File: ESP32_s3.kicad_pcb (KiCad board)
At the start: 2 copper layers, 72 parts, among them J11 backup, J13 Jetson Power Supply, J13 jetsonnano, J14 TXRX, J15 TXRX2, J3 Conn_01x02, J4 Servo motor, J5 PJ-040DH, J7 Conn_01x02, J8 Conn_01x02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

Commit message: update traces
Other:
- board outline added: 100 x 75 mm
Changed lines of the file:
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@@
 	)
 	(setup
+		(stackup
+			(layer "F.SilkS"
+				(type "Top Silk Screen")
+			)
+			(layer "F.Paste"
+				(type "Top Solder Paste")
+			)
+			(layer "F.Mask"
+				(type "Top Solder Mask")
+				(thickness 0.01)
+			)
+			(layer "F.Cu"
+				(type "copper")
+				(thickness 0.035)
+			)
+			(layer "dielectric 1"
+				(type "core")
+				(thickness 1.51)
+				(material "FR4")
+				(epsilon_r 4.5)
+				(loss_tangent 0.02)
+			)
+			(layer "B.Cu"
+				(type "copper")
+				(thickness 0.035)
+			)
+			(layer "B.Mask"
+				(type "Bottom Solder Mask")
+				(thickness 0.01)
+			)
+			(layer "B.Paste"
+				(type "Bottom Solder Paste")
+			)
+			(layer "B.SilkS"
+				(type "Bottom Silk Screen")
+			)
+			(copper_finish "None")
+			(dielectric_constraints no)
+		)
 		(pad_to_mask_clearance 0)
 		(allow_soldermask_bridges_in_footprints no)
@@
 		(descr "<B>WR-PHD </B><BR> 2.54mm Pin Header, 3 Pin")
 		(property "Reference" "J13"
-			(at -6.6096 -0.6625 0)
+			(at -5.31 0.02 0)
 			(layer "F.SilkS")
 			(effects
@@
 		(descr "<B>WR-PHD </B><BR> 2.54mm Pin Header, 3 Pin")
 		(property "Reference" "J4"
-			(at -6.6096 -0.6625 0)
+			(at -5.02 -0.48 0)
 			(layer "F.SilkS")
 			(effects
@@
 	)
 	(gr_rect
-		(start 105.46 55)
-		(end 205.46 130)
+		(start 105 55)
+		(end 205 130)
 		(stroke
-			(width 0.2)
+			(width 0.05)
 			(type default)
 		)
 		(fill none)
-		(layer "F.Cu")
-		(net 16)
+		(layer "Edge.Cuts")
 	)
 	(segment
@@
 		(start 112.34 116.615)
 		(end 112.34 115.447)
-		(width 0.2)
+		(width 0.254)
 		(layer "F.Cu")
 		(net 1)
@@
 		(start 112.34 118.115)
 		(end 112.34 116.615)
-		(width 0.2)
+		(width 0.254)
 		(layer "F.Cu")
 		(net 1)
@@
 		(start 112.34 116.615)
 		(end 110.84 115.115)
-		(width 0.2)
+		(width 0.381)
 		(layer "F.Cu")
 		(net 1)
@@
 		(start 130.46 70.375)
 		(end 123.8325 70.375)
-		(width 0.2)
+		(width 0.254)
 		(layer "F.Cu")
 		(net 2)
@@
 		(start 123.8325 70.375)
 		(end 119.9575 66.5)
-		(width 0.2)
+		(width 0.254)
 		(layer "F.Cu")
 		(net 2)
@@
 		(start 124.36 64.5)
 		(end 119.9575 64.5)
-		(width 0.2)
+		(width 0.254)
 		(layer "F.Cu")
 		(net 19)
@@
 		(start 130.46 66)
 		(end 130.46 68.5)
-		(width 0.2)
+		(width 0.254)
 		(layer "F.Cu")
 		(net 35)
@@
 		(start 126.96 64)
 		(end 126.46 64.5)
-		(width 0.2)
+		(width 0.381)
 		(layer "F.Cu")
 		(net 71)
@@
 		(start 130.46 64)
 		(end 130.46 58.5)
-		(width 0.2)
+		(width 0.381)
 		(layer "F.Cu")
 		(net 71)
@@
 		(start 130.46 64)
 		(end 126.96 64)
-		(width 0.2)
+		(width 0.381)
 		(layer "F.Cu")
 		(net 71)
@@
 		(start 130.46 58.5)
 		(end 133 58.5)
-		(width 0.2)
+		(width 0.381)
 		(layer "B.Cu")
 		(net 71)

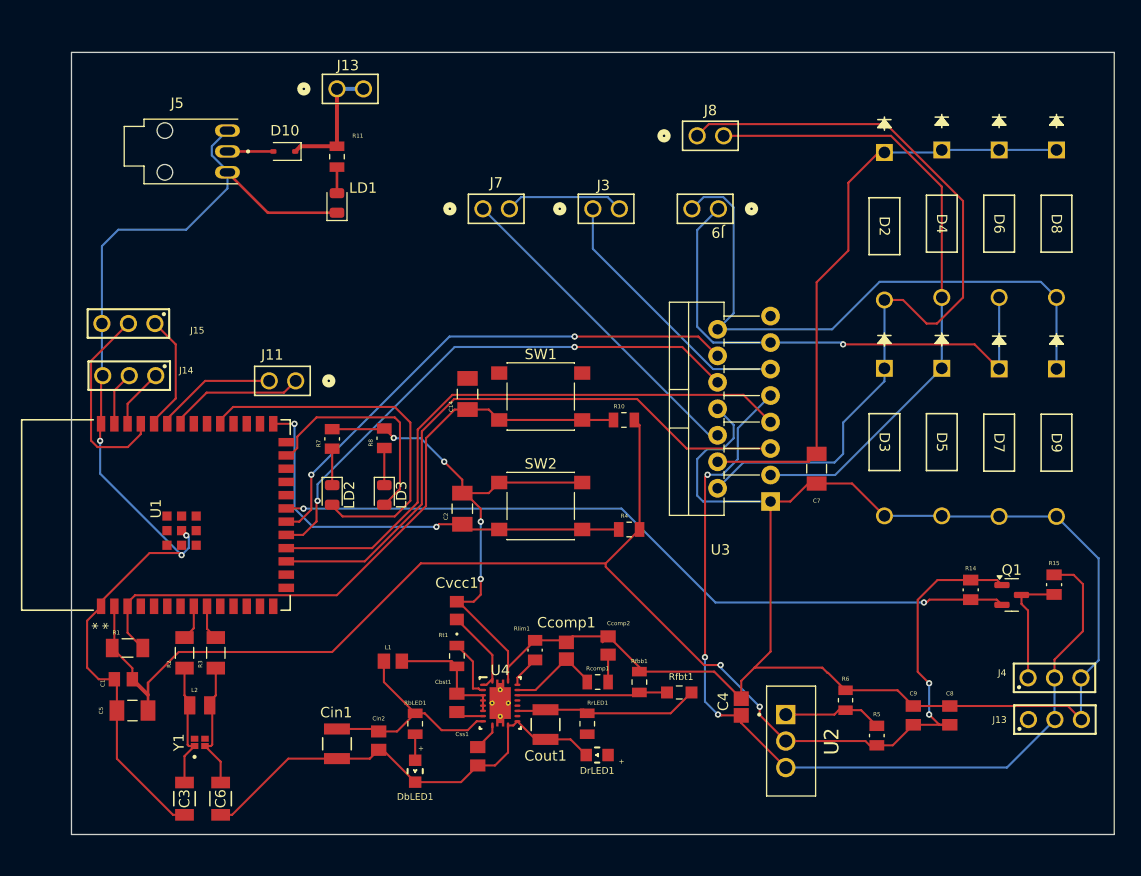
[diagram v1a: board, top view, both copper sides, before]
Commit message: update drill holes and name
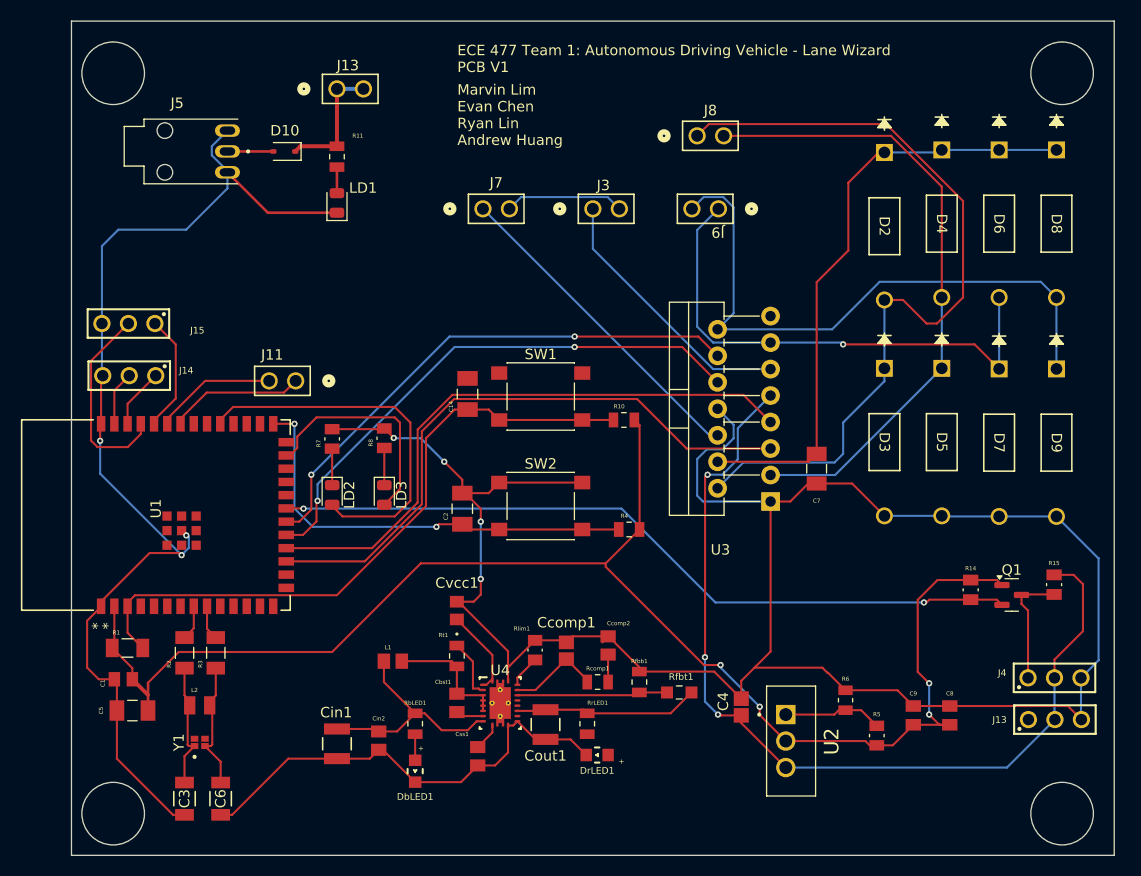
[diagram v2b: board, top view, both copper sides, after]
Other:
- board size 100 x 75 mm -> 100 x 80 mm
- board text added: "ECE 477 Team 1: Autonomous Driving Vehicle - Lane Wizard PCB V1"
- board text added: "Marvin Lim Evan Chen Ryan Lin Andrew Huang"
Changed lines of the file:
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@@
 		)
 	)
-	(gr_rect
-		(start 105 55)
-		(end 205 130)
+	(gr_circle
+		(center 109 128)
+		(end 112 128)
 		(stroke
 			(width 0.05)
@@
 		(layer "Edge.Cuts")
 	)
+	(gr_circle
+		(center 200 128)
+		(end 203 128)
+		(stroke
+			(width 0.05)
+			(type default)
+		)
+		(fill none)
+		(layer "Edge.Cuts")
+	)
+	(gr_circle
+		(center 200 57)
+		(end 203 57)
+		(stroke
+			(width 0.05)
+			(type default)
+		)
+		(fill none)
+		(layer "Edge.Cuts")
+	)
+	(gr_rect
+		(start 105 52)
+		(end 205 132)
+		(stroke
+			(width 0.05)
+			(type default)
+		)
+		(fill none)
+		(layer "Edge.Cuts")
+	)
+	(gr_circle
+		(center 109 57)
+		(end 112 57)
+		(stroke
+			(width 0.05)
+			(type default)
+		)
+		(fill none)
+		(layer "Edge.Cuts")
+	)
+	(gr_text "ECE 477 Team 1: Autonomous Driving Vehicle - Lane Wizard\nPCB V1\n"
+		(at 142 57 0)
+		(layer "F.SilkS")
+		(effects
+			(font
+				(size 1 1)
+				(thickness 0.1)
+			)
+			(justify left bottom)
+		)
+	)
+	(gr_text "Marvin Lim\nEvan Chen\nRyan Lin\nAndrew Huang"
+		(at 142 64 0)
+		(layer "F.SilkS")
+		(effects
+			(font
+				(size 1 1)
+				(thickness 0.1)
+			)
+			(justify left bottom)
+		)
+	)
 	(segment

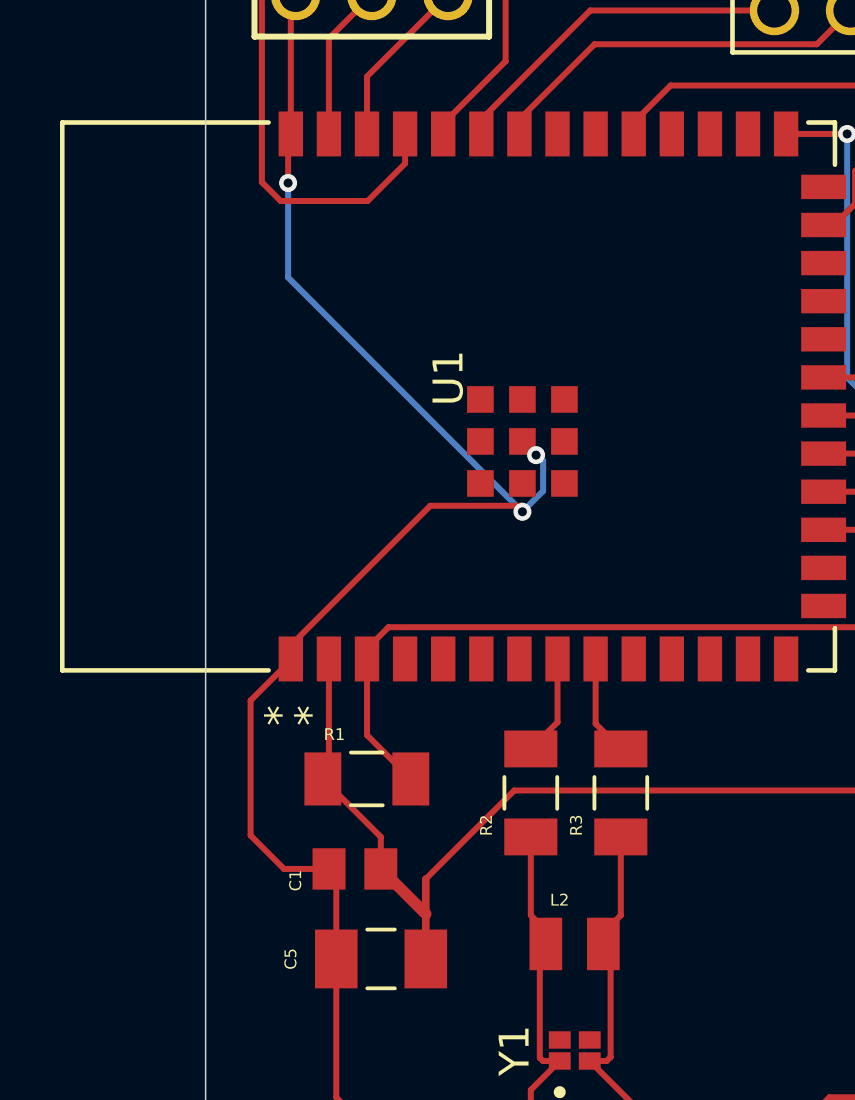
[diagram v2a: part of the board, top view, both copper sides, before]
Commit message: fix acute angles
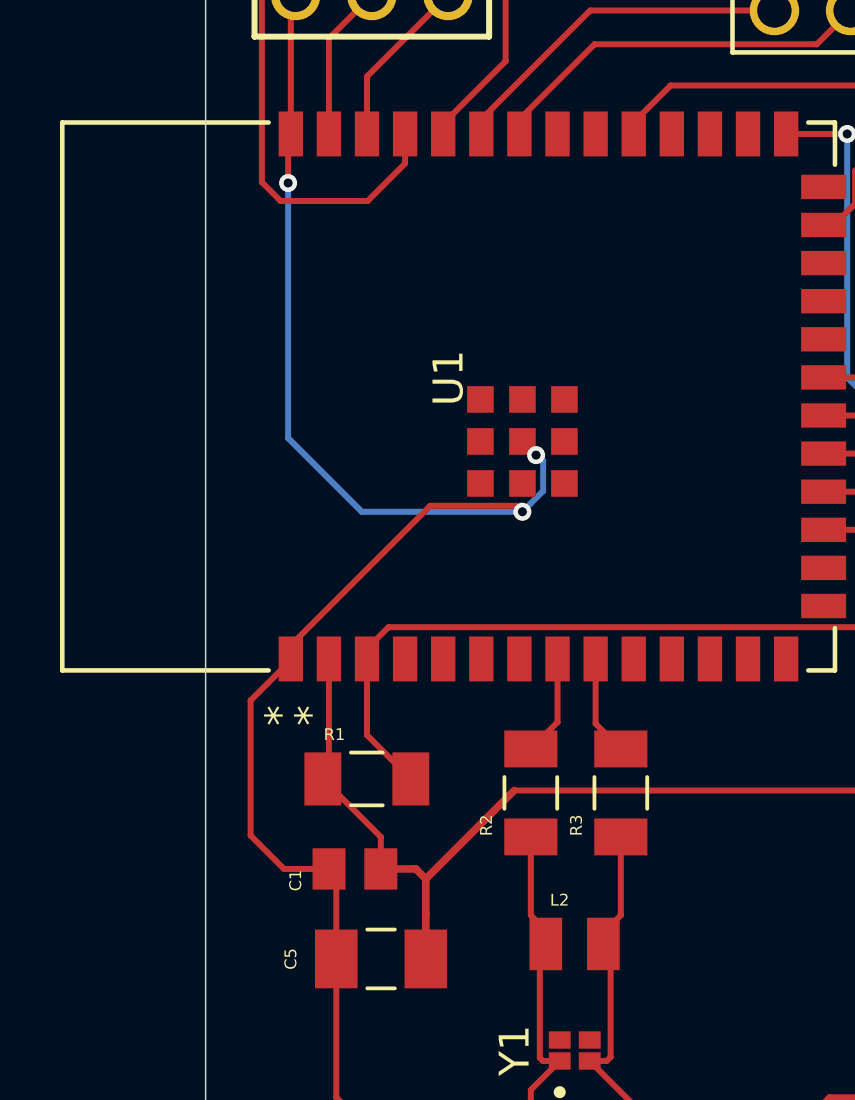
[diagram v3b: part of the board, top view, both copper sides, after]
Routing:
- net GND: track 351.1 -> 354.2 mm
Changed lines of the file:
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@@
+		)
+	)
+	(gr_text_box "Boost Voltage Regulator"
+		(start 141.5 126)
+		(end 162.5 129)
+		(layer "F.SilkS")
+		(effects
+			(font
+				(size 1 1)
+				(thickness 0.1)
+			)
+			(justify left top)
+		)
+		(border yes)
+		(stroke
+			(width 0.1)
+			(type solid)
+		)
+	)
+	(gr_text_box "micro"
+		(start 122.25 79)
+		(end 127.75 82)
+		(layer "F.SilkS")
+		(effects
+			(font
+				(size 1 1)
+				(thickness 0.1)
+			)
+			(justify left top)
+		)
+		(border yes)
+		(stroke
+			(width 0.1)
+			(type solid)
+		)
+	)
+	(gr_text_box "Logic Level Shifter"
+		(start 181 101)
+		(end 198 104)
+		(layer "F.SilkS")
+		(effects
+			(font
+				(size 1 1)
+				(thickness 0.1)
+			)
+			(justify left top)
+		)
+		(border yes)
+		(stroke
+			(width 0.1)
+			(type solid)
+		)
+	)
+	(gr_text_box "Switch"
+		(start 145 79)
+		(end 151 82)
+		(layer "F.SilkS")
+		(effects
+			(font
+				(size 1 1)
+				(thickness 0.1)
+			)
+			(justify left top)
+		)
+		(border yes)
+		(stroke
+			(width 0.1)
+			(type solid)
+		)
+	)
+	(gr_text_box "Power Supply"
+		(start 114.5 55)
+		(end 126.5 58)
+		(layer "F.SilkS")
+		(effects
+			(font
+				(size 1 1)
+				(thickness 0.1)
+			)
+			(justify left top)
+		)
+		(border yes)
+		(stroke
+			(width 0.1)
+			(type solid)
+		)
+	)
+	(gr_text_box "H-Bridge"
+		(start 164.5 74)
+		(end 173.5 77)
+		(layer "F.SilkS")
+		(effects
+			(font
+				(size 1 1)
+				(thickness 0.1)
+			)
+			(justify left top)
+		)
+		(border yes)
+		(stroke
+			(width 0.1)
+			(type solid)
+		)
+	)
+	(gr_text_box "Low Dropout"
+		(start 178 126)
+		(end 189 129)
+		(layer "F.SilkS")
+		(effects
+			(font
+				(size 1 1)
+				(thickness 0.1)
+			)
+			(justify left top)
+		)
+		(border yes)
+		(stroke
+			(width 0.1)
+			(type solid)
 		)
 	)
@@
 		(end 109.11 108.115)
 		(width 0.2)
+		(layer "F.Cu")
+		(net 1)
+	)
+	(segment
+		(start 112.008 115.115)
+		(end 112.34 115.447)
+		(width 0.254)
 		(layer "F.Cu")
 		(net 1)
@@
 		(start 112.34 115.447)
 		(end 115.287 112.5)
-		(width 0.2)
+		(width 0.254)
 		(layer "F.Cu")
 		(net 1)
@@
 		(end 181.55 121.45)
 		(width 0.2)
+		(layer "F.Cu")
+		(net 1)
+	)
+	(segment
+		(start 110.84 115.115)
+		(end 112.008 115.115)
+		(width 0.254)
 		(layer "F.Cu")
 		(net 1)
@@
 		(end 194.23 106.08)
 		(width 0.2)
-		(layer "F.Cu")
-		(net 1)
-	)
-	(segment
-		(start 112.34 116.615)
-		(end 110.84 115.115)
-		(width 0.381)
 		(layer "F.Cu")
 		(net 1)
@@
 	)
 	(segment
+		(start 107.75 100.75)
+		(end 110.209502 103.209502)
+		(width 0.2)
+		(layer "B.Cu")
+		(net 2)
+	)
+	(segment
 		(start 118.4575 64)
 		(end 119.9575 62.5)
@@
 	)
 	(segment
-		(start 115.56 103.209502)
-		(end 107.75 95.399502)
-		(width 0.2)
-		(layer "B.Cu")
-		(net 2)
-	)
-	(segment
 		(start 140.75 94.25)
 		(end 138.5 92)
@@
 	)
 	(segment
+		(start 110.209502 103.209502)
+		(end 115.56 103.209502)
+		(width 0.2)
+		(layer "B.Cu")
+		(net 2)
+	)
+	(segment
 		(start 138.5 92)
 		(end 135.927493 92)
@@
 	)
 	(segment
-		(start 107.75 95.399502)
-		(end 107.75 92.25)
-		(width 0.2)
-		(layer "B.Cu")
-		(net 2)
-	)
-	(segment
 		(start 109.5 72)
 		(end 116 72)
 		(width 0.2)
 		(layer "B.Cu")
+		(net 2)
+	)
+	(segment
+		(start 107.75 92.25)
+		(end 107.75 100.75)
+		(width 0.2)
+		(layer "B.Cu")

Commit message: update traces
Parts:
- moved RrLED1 3.54 mm to (158.0, 119.2)
- moved DrLED1 2.60 mm to (154.2, 120.0), turned to 90 degrees
- moved RbLED1 1.62 mm to (138.0, 121.0)
- moved DbLED1 1.52 mm to (138.0, 125.5)
- moved R6 1.38 mm to (179.2, 118.5)
- moved Cbst1 0.50 mm to (142.0, 116.9)
- moved C3 0.34 mm to (115.5, 126.5)
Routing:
- net Net-(DrLED1-A): track 0.00 -> 4.27 mm
- net GND: track 354.2 -> 357.8 mm
- net Vin: track 22.1 -> 21.5 mm
- net +3.3V: track 140.9 -> 141.4 mm
- added copper zone on F.Cu, net +3.3V
- added copper zone on F.Cu, net +5V
- added copper zone on F.Cu, net GND
- added copper zone on F.Cu, net Vin
- added copper zone on F.Cu, net Vout

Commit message: add pig
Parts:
- moved LD1 7.22 mm to (123.2, 69.0)
- moved R11 7.22 mm to (123.2, 64.6)
- moved D10 7.22 mm to (118.2, 64.1)
- moved J13 6.77 mm to (130.0, 65.2)
- moved J5 6.48 mm to (113.5, 64.0)
- moved J8 6.39 mm to (171.2, 64.5)
- moved C6 0.30 mm to (119.0, 126.5)
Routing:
- net GND: track 357.8 -> 351.4 mm
- net Net-(D4-A): track 61.0 -> 55.4 mm
- net Net-(D2-A): track 77.6 -> 72.1 mm
- net 5V: track 12.2 -> 14.2 mm
- net Net-(D10-A): track 4.40 -> 3.68 mm
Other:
- outline, holes or cut-outs redrawn

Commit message: fix error
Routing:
- net GND: track 351.4 -> 381.4 mm, vias 7 -> 11
- net Vout: track 17.6 -> 18.6 mm

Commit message: update schematic and PCB
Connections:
- C7 pad 1: +12V -> Vout
- D2 pad 1: +12V -> Vout
- D4 pad 1: +12V -> Vout
- D6 pad 1: +12V -> Vout
- D8 pad 1: +12V -> Vout
- U3 pad 4: +12V -> Vout
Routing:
- net Vout: track 18.6 -> 100.8 mm, vias 0 -> 2
- net +12V: track 58.3 -> 0.00 mm

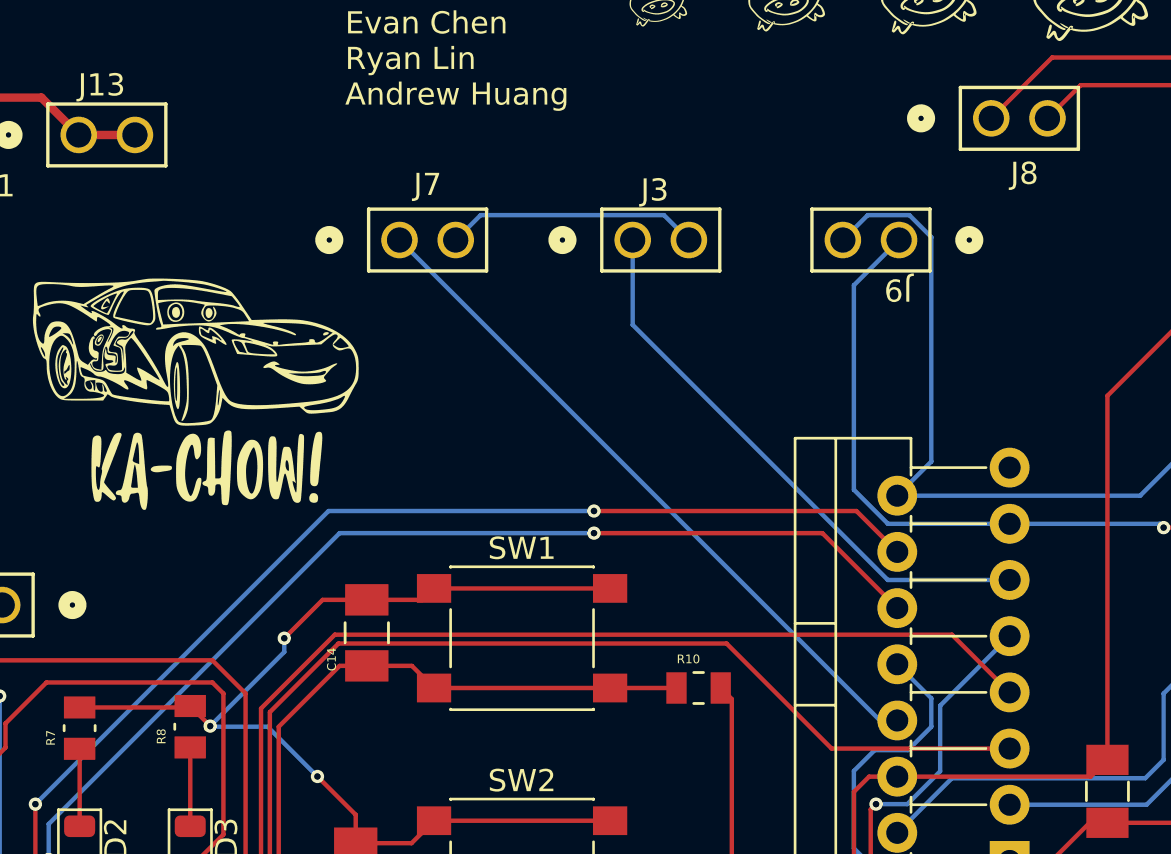
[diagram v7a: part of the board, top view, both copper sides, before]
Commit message: update labels and traces
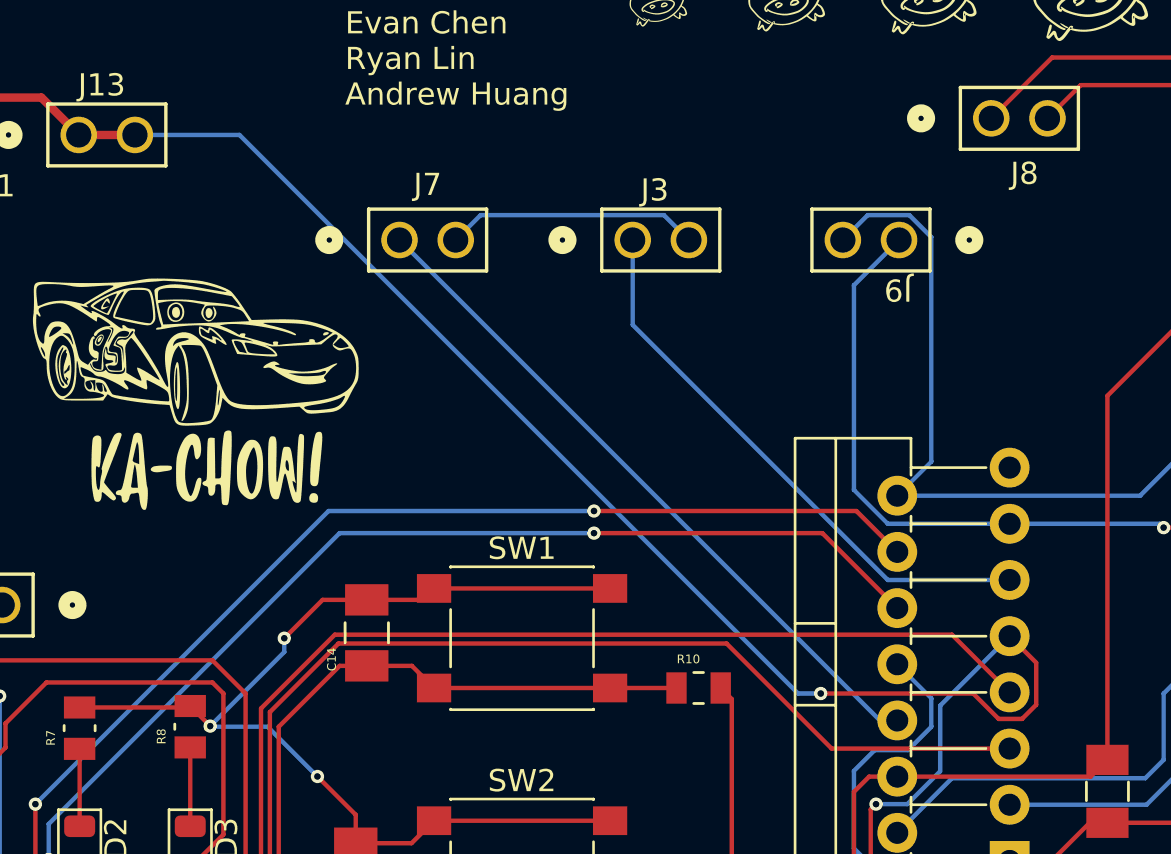
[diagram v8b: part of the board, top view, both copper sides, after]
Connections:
- net +3.3V renamed 3.3V
- net Vout renamed 8V
- C4 pad 1: +5V -> 5V
- Cin1 pad 1: Vin -> 5V
- Cin2 pad 1: Vin -> 5V
- J4 pad 2: +5V -> 5V
- L1 pad 1: Vin -> 5V
- R15 pad 2: +5V -> 5V
- RbLED1 pad 1: Vin -> 5V
- U2 pad 3: +5V -> 5V
- U3 pad 9: +5V -> 5V
- U4 pad 9: Vin -> 5V
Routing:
- net 5V: track 14.2 -> 91.1 mm, vias 0 -> 4
- net Vin: track 21.5 -> 0.00 mm
- net +5V: vias 3 -> 0
- added copper zone on F.Cu, net 5V
- removed copper zone on F.Cu, net +5V
- removed copper zone on F.Cu, net Vin
